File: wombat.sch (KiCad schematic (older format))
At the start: 188 parts, among them J1 Conn_01x01, J2 Conn_01x01, SW1 SW_SPST, SW10 SW_SPST, SW101 SW_Push, SW11 SW_SPST, SW12 SW_SPST, SW13 SW_SPST, SW14 SW_SPST, SW15 SW_SPST, SW16 SW_SPST, SW17 SW_SPST, SW18 SW_SPST, SW19 SW_SPST, SW2 SW_SPST, SW20 SW_SPST, SW21 SW_SPST, SW22 SW_SPST, SW23 SW_SPST, SW24 SW_SPST, SW25 SW_SPST, SW26 SW_SPST, SW27 SW_SPST, SW28 SW_SPST, SW29 SW_SPST, SW3 SW_SPST, SW30 SW_SPST, SW31 SW_SPST, SW32 SW_SPST, SW33 SW_SPST, SW34 SW_SPST, SW35 SW_SPST, SW36 SW_SPST, SW37 SW_SPST, SW38 SW_SPST, SW39 SW_SPST, SW4 SW_SPST, SW40 SW_SPST, SW41 SW_SPST, SW42 SW_SPST, SW43 SW_SPST, SW44 SW_SPST, SW45 SW_SPST, SW46 SW_SPST, SW5 SW_SPST, SW6 SW_SPST, SW7 SW_SPST, SW8 SW_SPST, SW9 SW_SPST, U1 ProMicro

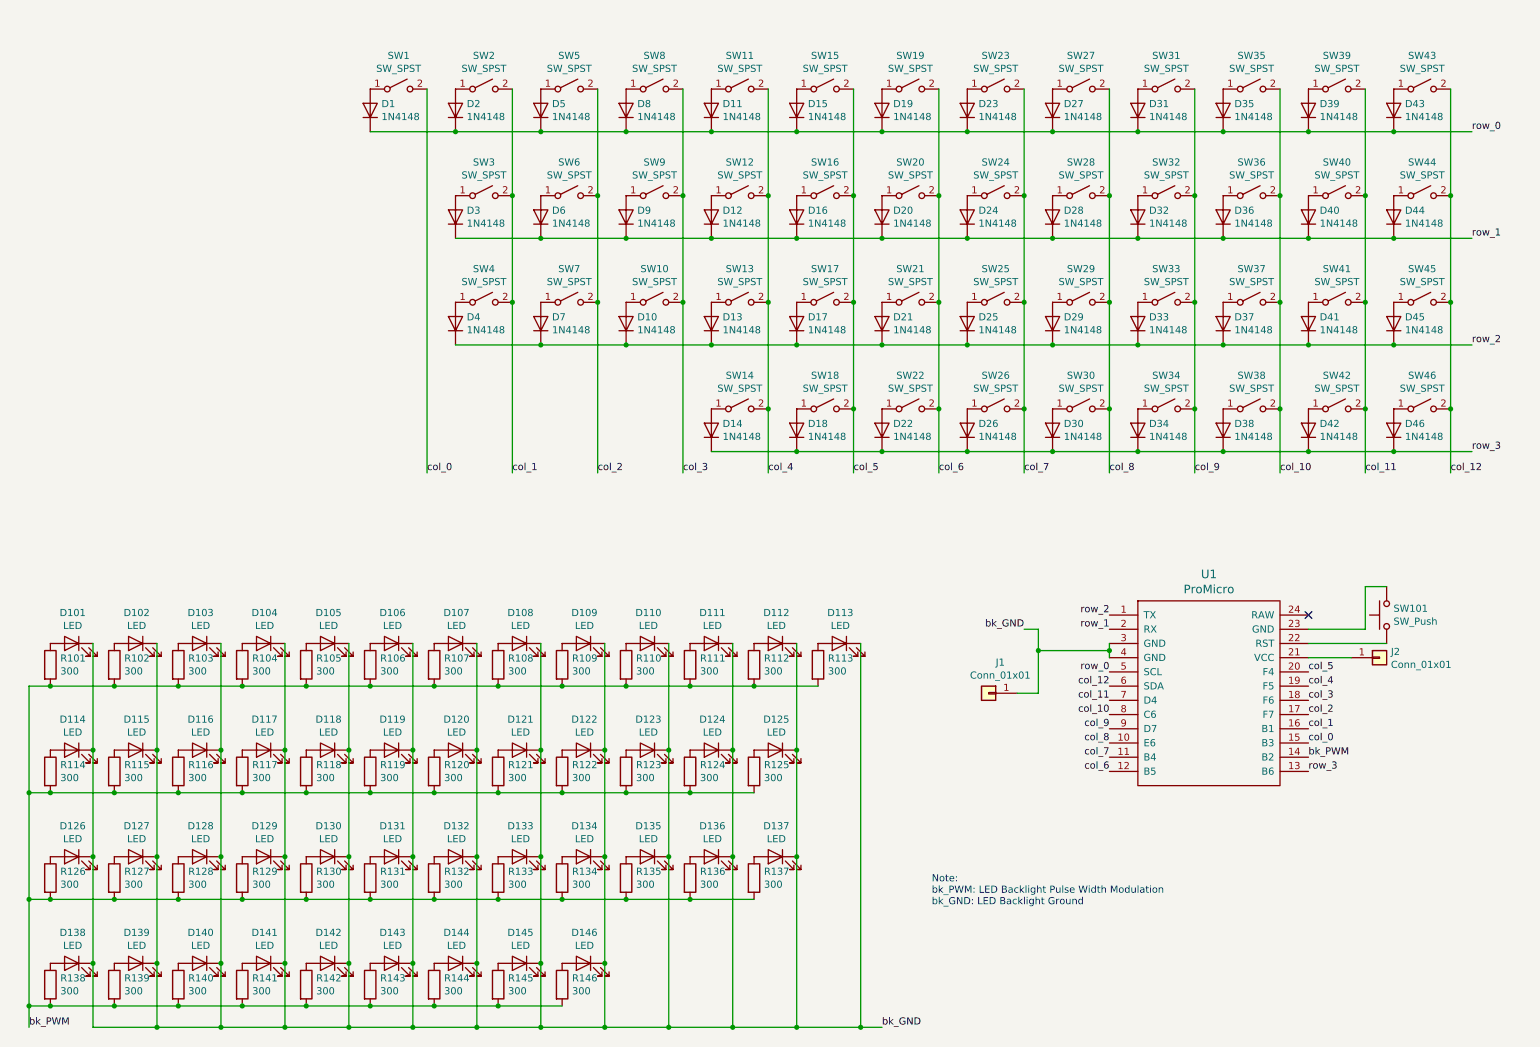
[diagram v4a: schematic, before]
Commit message: Support bottom row variant
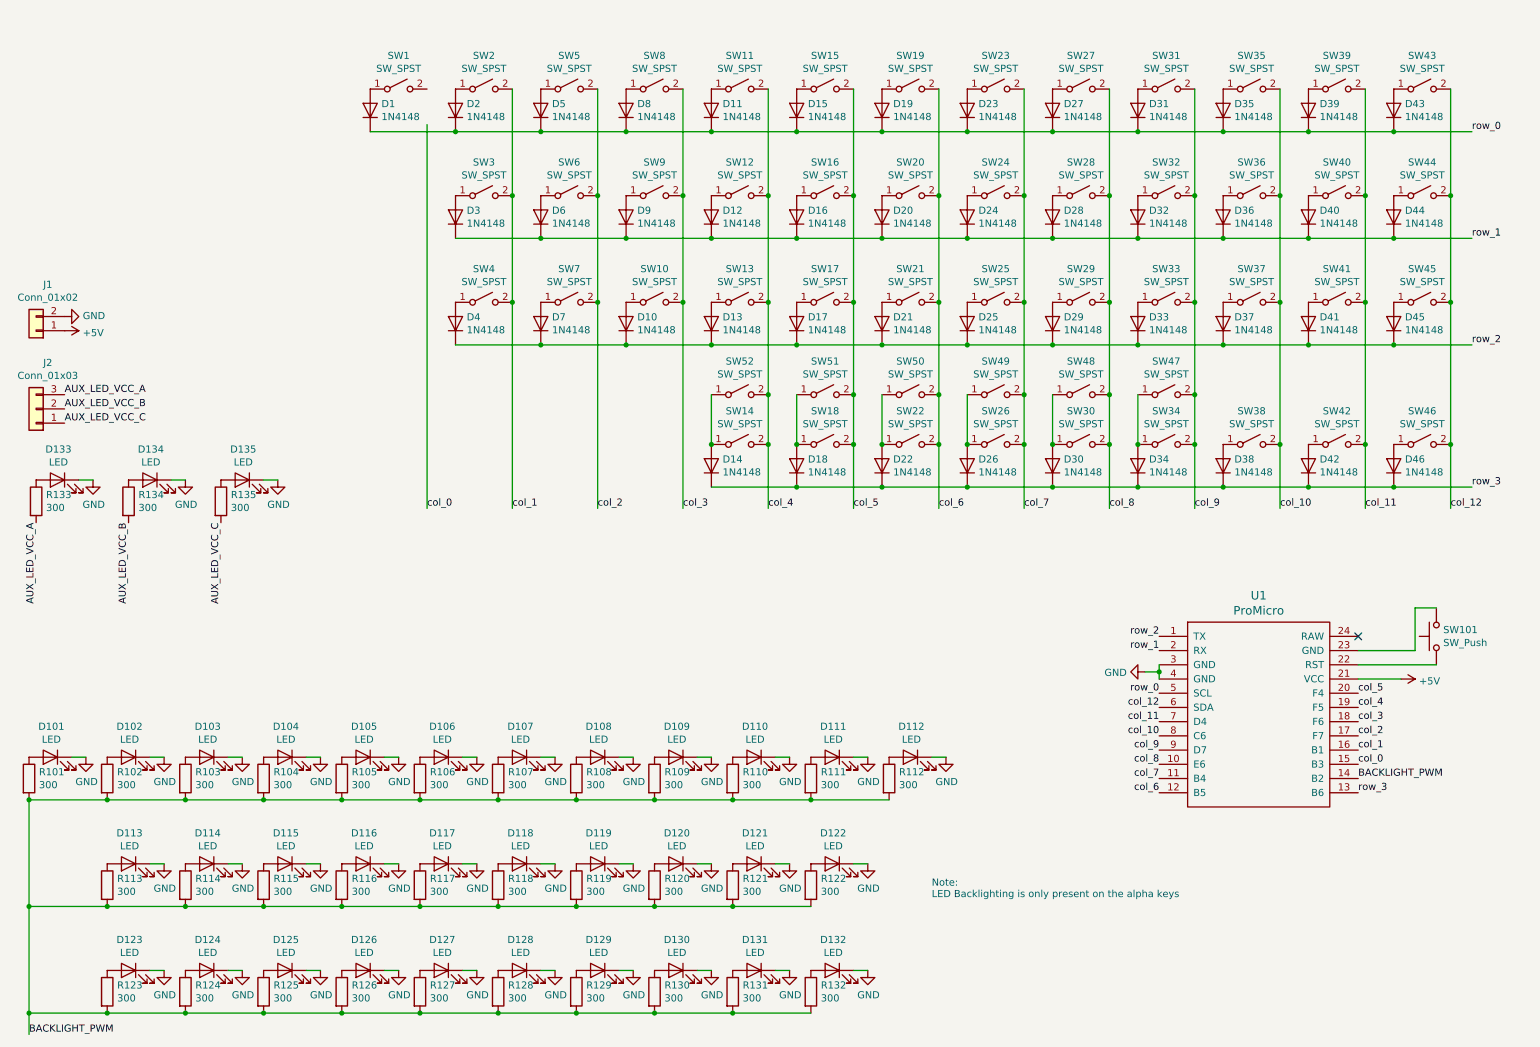
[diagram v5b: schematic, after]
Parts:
- removed D113, D114, D125, D126, D137, D138, D139, D140, D141, D142, D143, D144, D145, D146: LED, keebs-github:LED_D2.0mm_W4.8mm_H2.5mm_FlatTop_Reverse_Polarity, symbol Device:LED
- removed J1, J2: Conn_01x01, Connector_Wire:SolderWirePad_1x01_Drill0.8mm, symbol Connector_Generic:Conn_01x01
- removed R113, R114, R125, R126, R137, R138, R139, R140, R141, R142, R143, R144, R145, R146: 300, Resistor_SMD:R_0805_2012Metric_Pad1.15x1.40mm_HandSolder, symbol Device:R
- added D133, D134, D135: LED, keebs-github:LED_D2.0mm_W4.8mm_H2.5mm_FlatTop_Reverse_Polarity, symbol Device:LED
- added J1: Conn_01x02, Connector_Wire:SolderWirePad_1x02_P3.81mm_Drill1.2mm, symbol Connector_Generic:Conn_01x02
- added J2: Conn_01x03, Connector_Wire:SolderWirePad_1x03_P3.81mm_Drill1.2mm, symbol Connector_Generic:Conn_01x03
- added R133, R134, R135: 300, Resistor_SMD:R_0805_2012Metric_Pad1.15x1.40mm_HandSolder, symbol Device:R
- added SW47: SW_SPST, keebs-github:Mx_Alps_200, symbol Switch:SW_SPST
- added SW48: SW_SPST, keebs-github:Mx_Alps_225, symbol Switch:SW_SPST
- added SW49, SW50, SW51, SW52: SW_SPST, keebs-github:Mx_Alps_125, symbol Switch:SW_SPST
- D10, D11, D12, D13, D14, D15, D16, D17, D18, D19, D2, D20, D21, D22, D23, D24, D25, D26, D27, D28, D29, D3, D30, D31, D32, D33, D34, D35, D36, D37, D38, D39, D4, D40, D41, D42, D43, D44, D45, D46, D5, D6, D7, D8, D9: footprint Diode_SMD:D_SOD-123 -> Diode_SMD:D_0805_2012Metric_Pad1.15x1.40mm_HandSolder
- renumbered D115 to D113, D116 to D114, D117 to D115, D118 to D116, D119 to D117, D120 to D118, D121 to D119, D122 to D120, D123 to D121, D124 to D122, D127 to D123, D128 to D124, D129 to D125, D130 to D126, D131 to D127, D132 to D128, D133 to D129, D134 to D130, D135 to D131, D136 to D132, R115 to R113, R116 to R114, R117 to R115, R118 to R116, R119 to R117, R120 to R118, R121 to R119, R122 to R120, R123 to R121, R124 to R122, R127 to R123, R128 to R124, R129 to R125, R130 to R126, R131 to R127, R132 to R128, R133 to R129, R134 to R130, R135 to R131, R136 to R132
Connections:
- net col_0: no longer SW1.2 (B)
- net col_4: now also SW52.2 (B)
- net col_5: now also SW51.2 (B)
- net col_6: now also SW50.2 (B)
- net col_7: now also SW49.2 (B)
- net col_8: now also SW48.2 (B)
- net col_9: now also SW47.2 (B)
- net +5V: now reaches U1.21 (VCC)
- net +5V: now also J1.1 (Pin_1)
- net at D14.2 (A), SW14.1 (A): now also SW52.1 (A)
- net at D18.2 (A), SW18.1 (A): now also SW51.1 (A)
- net at D22.2 (A), SW22.1 (A): now also SW50.1 (A)
- net at D26.2 (A), SW26.1 (A): now also SW49.1 (A)
- net at D30.2 (A), SW30.1 (A): now also SW48.1 (A)
- net at D34.2 (A), SW34.1 (A): now also SW47.1 (A)
- net bk_GND renamed GND
- net GND: now also D133.1 (K), D134.1 (K), D135.1 (K), J1.2 (Pin_2)
- net bk_PWM renamed BACKLIGHT_PWM
- new net: D134.2 (A), R134.1
- new net: D133.2 (A), R133.1
- new net: D135.2 (A), R135.1
- new net AUX_LED_VCC_A: J2.3 (Pin_3), R133.2
- new net AUX_LED_VCC_B: J2.2 (Pin_2), R134.2
- new net AUX_LED_VCC_C: J2.1 (Pin_1), R135.2
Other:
- note added: "Note:\nLED Backlighting is only present on the alpha keys"
- note removed: "Note:\nbk_PWM: LED Backlight Pulse Width Modulation\nbk_GND: LED Backlight Ground"
- moved on the sheet: D101, D102, D103, D104, D105, D106, D107, D108, D109, D110, D111, D112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

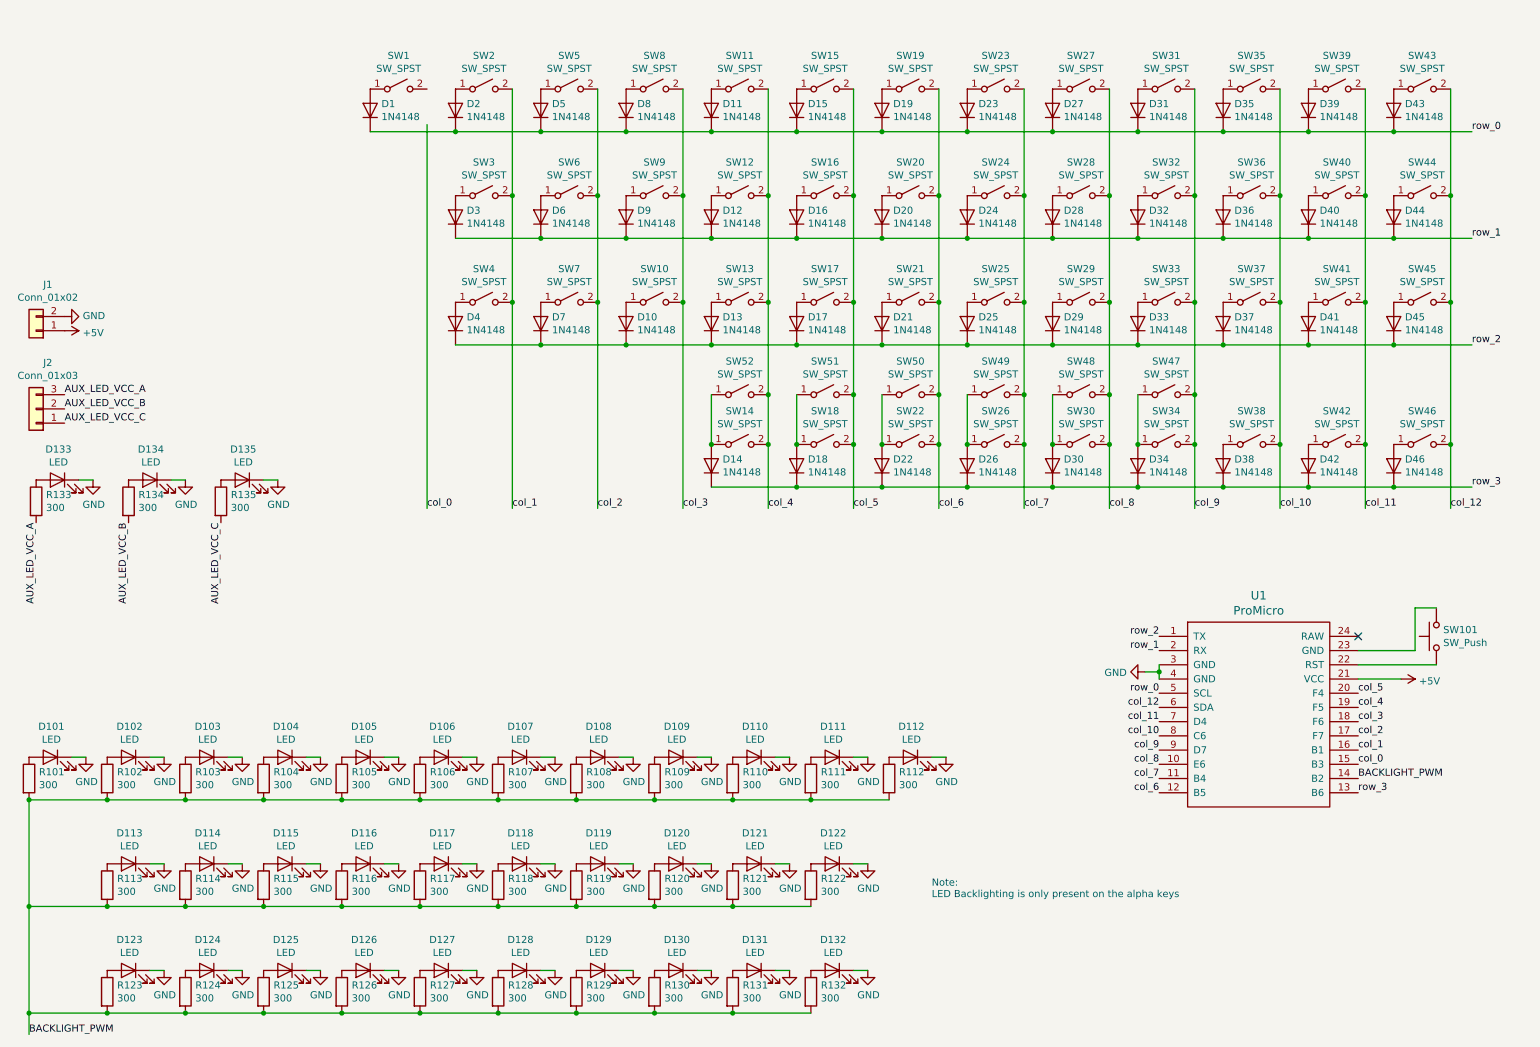
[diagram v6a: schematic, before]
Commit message: Prep for routing
- North facing LEDs
- invert stabilizers
- New mounting holes (it's overkill, but i'd rather have options)
- implemented transitor to drive LEDs
- rename lib dir to wombat.pretty
- map pinouts for capslock and layer indicator LEDs
- implement breakaway tab with LED indicators
- reorient resistor placement
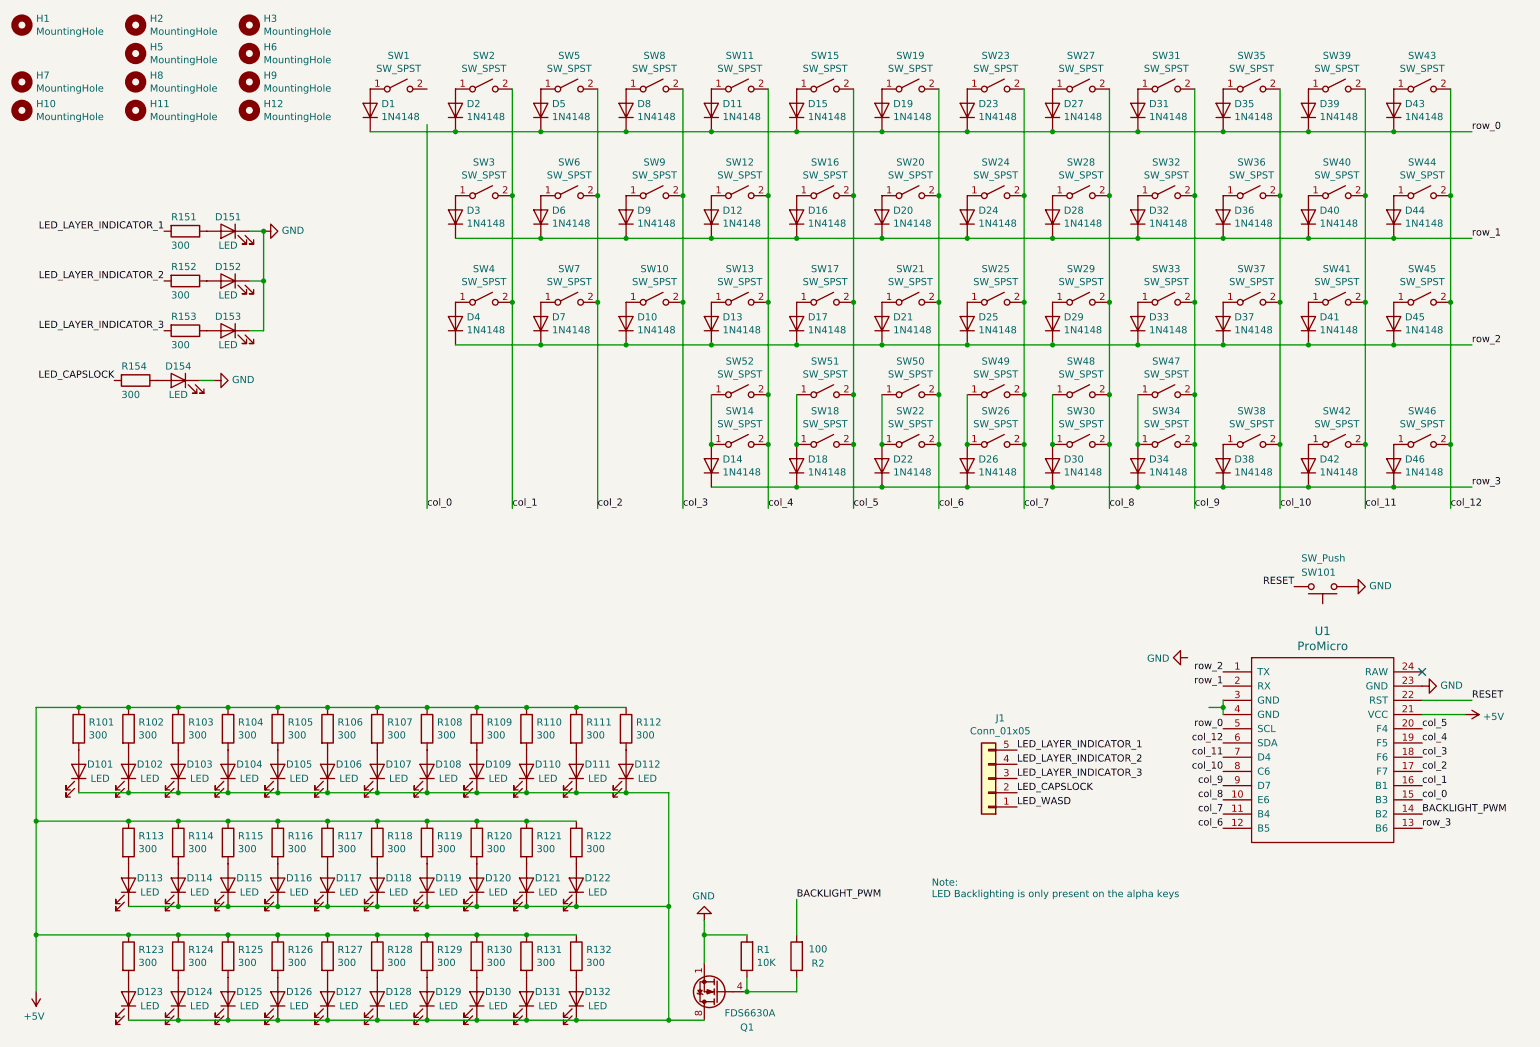
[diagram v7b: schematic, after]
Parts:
- removed D133, D134, D135: LED, keebs-github:LED_D2.0mm_W4.8mm_H2.5mm_FlatTop_Reverse_Polarity, symbol Device:LED
- removed J1: Conn_01x02, Connector_Wire:SolderWirePad_1x02_P3.81mm_Drill1.2mm, symbol Connector_Generic:Conn_01x02
- removed J2: Conn_01x03, Connector_Wire:SolderWirePad_1x03_P3.81mm_Drill1.2mm, symbol Connector_Generic:Conn_01x03
- removed R133, R134, R135: 300, Resistor_SMD:R_0805_2012Metric_Pad1.15x1.40mm_HandSolder, symbol Device:R
- added D151, D152, D153: LED, LED_SMD:LED_0805_2012Metric_Pad1.15x1.40mm_HandSolder, symbol Device:LED
- added D154: LED, wombat.pretty:LED_D2.0mm_W4.8mm_H2.5mm_FlatTop_Reverse_Polarity, symbol Device:LED
- added H1, H10, H11, H12, H2, H3, H5, H6, H7, H8, H9: MountingHole, wombat.pretty:MountingHole_2.2mm_M2_DIN965_Pad_Oval, symbol Mechanical:MountingHole
- added J1: Conn_01x05, Connector_PinSocket_2.00mm:PinSocket_1x05_P2.00mm_Vertical, symbol Connector_Generic:Conn_01x05
- added Q1: FDS6630A, Package_SO:SOIC-8_3.9x4.9mm_P1.27mm, symbol Transistor_FET:FDS6630A
- added R1: 10K, Resistor_SMD:R_0805_2012Metric_Pad1.15x1.40mm_HandSolder, symbol Device:R
- added R151, R152, R153: 300, Resistor_SMD:R_0805_2012Metric_Pad1.15x1.40mm_HandSolder, symbol Device:R
- added R154: 300, wombat.pretty:R_0805_2012Metric_Pad1.15x1.40mm_HandSolder_Double_Sided, symbol Device:R
- added R2: 100, Resistor_SMD:R_0805_2012Metric_Pad1.15x1.40mm_HandSolder, symbol Device:R
- D101, D102, D103, D104, D105, D106, D107, D108, D109, D110, D111, D112, D113, D114, D115, D116, D117, D118, D119, D120, D121, D122, D123, D124, D125, D126, D127, D128, D129, D130, D131, D132: footprint keebs-github:LED_D2.0mm_W4.8mm_H2.5mm_FlatTop_Reverse_Polarity -> wombat.pretty:LED_D2.0mm_W4.8mm_H2.5mm_FlatTop_Reverse_Polarity
- SW30, SW34: footprint keebs-github:Mx_Alps_225 -> wombat.pretty:Mx_Alps_225_Inverted_Stabs
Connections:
- net +5V: now also R101.1, R102.1, R103.1, R104.1, R105.1, R106.1, R107.1, R108.1, R109.1, R110.1, R111.1, R112.1, R113.1, R114.1, R115.1, R116.1, R117.1, R118.1, R119.1, R120.1, R121.1, R122.1, R123.1, R124.1, R125.1, R126.1, R127.1, R128.1, R129.1, R130.1, R131.1, R132.1
- net BACKLIGHT_PWM: now also R2.2; no longer R101.2, R102.2, R103.2, R104.2, R105.2, R106.2, R107.2, R108.2, R109.2, R110.2, R111.2, R112.2, R113.2, R114.2, R115.2, R116.2, R117.2, R118.2, R119.2, R120.2, R121.2, R122.2, R123.2, R124.2, R125.2, R126.2, R127.2, R128.2, R129.2, R130.2, R131.2, R132.2
- net GND: now also SW101.1, U1.23 (GND), D151.1 (K), D152.1 (K), D153.1 (K), D154.1 (K), Q1.1 (S), Q1.2 (S), Q1.3 (S), R1.2; no longer D101.1 (K), D102.1 (K), D103.1 (K), D104.1 (K), D105.1 (K), D106.1 (K), D107.1 (K), D108.1 (K), D109.1 (K), D110.1 (K), D111.1 (K), D112.1 (K), D113.1 (K), D114.1 (K), D115.1 (K), D116.1 (K), D117.1 (K), D118.1 (K), D119.1 (K), D120.1 (K), D121.1 (K), D122.1 (K), D123.1 (K), D124.1 (K), D125.1 (K), D126.1 (K), D127.1 (K), D128.1 (K), D129.1 (K), D130.1 (K), D131.1 (K), D132.1 (K), U1.3 (GND), U1.4 (GND)
- net at D101.2 (A): now also R101.2; no longer R101.1
- net at D102.2 (A): now also R102.2; no longer R102.1
- net at D103.2 (A): now also R103.2; no longer R103.1
- net at D104.2 (A): now also R104.2; no longer R104.1
- net at D105.2 (A): now also R105.2; no longer R105.1
- net at D106.2 (A): now also R106.2; no longer R106.1
- net at D107.2 (A): now also R107.2; no longer R107.1
- net at D108.2 (A): now also R108.2; no longer R108.1
- net at D109.2 (A): now also R109.2; no longer R109.1
- net at D110.2 (A): now also R110.2; no longer R110.1
- net at D111.2 (A): now also R111.2; no longer R111.1
- net at D112.2 (A): now also R112.2; no longer R112.1
- net RESET: now reaches U1.22 (RST)
- net RESET: now also SW101.2; no longer SW101.1
- net at D122.2 (A): now also R122.2; no longer R122.1
- net at D120.2 (A): now also R120.2; no longer R120.1
- net at D119.2 (A): now also R119.2; no longer R119.1
- net at D118.2 (A): now also R118.2; no longer R118.1
- net at D117.2 (A): now also R117.2; no longer R117.1
- net at D116.2 (A): now also R116.2; no longer R116.1
- net at D115.2 (A): now also R115.2; no longer R115.1
- net at D113.2 (A): now also R113.2; no longer R113.1
- net at D114.2 (A): now also R114.2; no longer R114.1
- net at D121.2 (A): now also R121.2; no longer R121.1
- net at D132.2 (A): now also R132.2; no longer R132.1
- net at D130.2 (A): now also R130.2; no longer R130.1
- net at D129.2 (A): now also R129.2; no longer R129.1
- net at D128.2 (A): now also R128.2; no longer R128.1
- net at D127.2 (A): now also R127.2; no longer R127.1
- net at D126.2 (A): now also R126.2; no longer R126.1
- net at D125.2 (A): now also R125.2; no longer R125.1
- net at D123.2 (A): now also R123.2; no longer R123.1
- net at D124.2 (A): now also R124.2; no longer R124.1
- net at D131.2 (A): now also R131.2; no longer R131.1
- new net: U1.3 (GND), U1.4 (GND)
- new net: D101.1 (K), D102.1 (K), D103.1 (K), D104.1 (K), D105.1 (K), D106.1 (K), D107.1 (K), D108.1 (K), D109.1 (K), D110.1 (K), D111.1 (K), D112.1 (K), D113.1 (K), D114.1 (K), D115.1 (K), D116.1 (K), D117.1 (K), D118.1 (K), D119.1 (K), D120.1 (K), D121.1 (K), D122.1 (K), D123.1 (K), D124.1 (K), D125.1 (K), D126.1 (K), D127.1 (K), D128.1 (K), D129.1 (K), D130.1 (K), D131.1 (K), D132.1 (K), Q1.5 (D), Q1.6 (D), Q1.7 (D), Q1.8 (D)
- new net: D153.2 (A), R153.1
- new net: D152.2 (A), R152.1
- new net: D151.2 (A), R151.1
- new net: Q1.4 (G), R1.1, R2.1
- new net: D154.2 (A), R154.1
- new net LED_CAPSLOCK: J1.2 (Pin_2), R154.2
- new net LED_LAYER_INDICATOR_1: J1.5 (Pin_5), R151.2
- new net LED_LAYER_INDICATOR_2: J1.4 (Pin_4), R152.2
- new net LED_LAYER_INDICATOR_3: J1.3 (Pin_3), R153.2
- new net LED_WASD: J1.1 (Pin_1)
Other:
- moved on the sheet: SW101, U1
